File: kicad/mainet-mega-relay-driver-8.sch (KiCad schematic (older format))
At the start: 8 parts, among them J37 Screw_Terminal_01x03, K8 SANYOU_SRD_Form_C, Q8 2N3904, U9 4N37

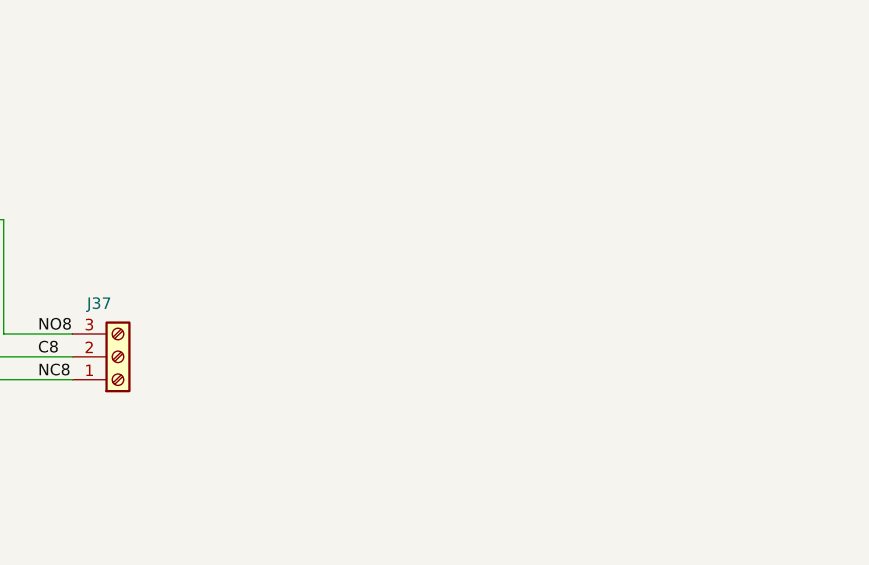
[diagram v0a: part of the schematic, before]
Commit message: KICAD: Agregar .sch para usar  el relé 8 para inhibir el M400  desde el software
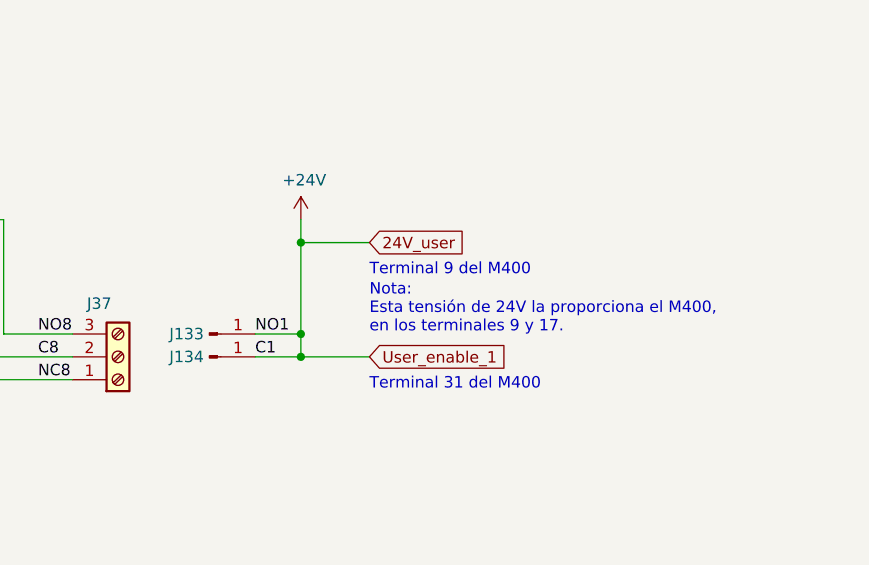
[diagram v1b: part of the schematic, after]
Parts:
- added J133, J134: Conn_01x01_Male, symbol Connector:Conn_01x01_Male
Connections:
- new net +24V: J133.1 (Pin_1), J134.1 (Pin_1)
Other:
- note added: "Nota:\nEsta tensión de 24V la proporciona el M400, \nen los terminales 9 y 17."
- note added: "Terminal 31 del M400"
- note added: "Terminal 9 del M400"
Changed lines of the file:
@@
 Text Notes 6000 5000 0    50   ~ 0
 Relay Ground\nNo conectar a la tierra\ndel Arduino Mega\n
+$Comp
+L Connector:Conn_01x01_Male J?
+U 1 1 6106E50A
+P 8550 3800
+AR Path="/5FC25793/5FD90A95/6106E50A" Ref="J?"  Part="1"
+AR Path="/5FC25793/5FD90D3E/6106E50A" Ref="J?"  Part="1"
+AR Path="/5FC25793/5FD92195/6106E50A" Ref="J133"  Part="1"
+F 0 "J133" H 8450 3800 50  0000 C CNN
+F 1 "Conn_01x01_Male" H 8658 3890 50  0001 C CNN
+F 2 "" H 8550 3800 50  0001 C CNN
+F 3 "~" H 8550 3800 50  0001 C CNN
+	1    8550 3800
+	1    0    0    -1
+$EndComp
+$Comp
+L Connector:Conn_01x01_Male J?
+U 1 1 6106E510
+P 8550 3900
+AR Path="/5FC25793/5FD90A95/6106E510" Ref="J?"  Part="1"
+AR Path="/5FC25793/5FD90D3E/6106E510" Ref="J?"  Part="1"
+AR Path="/5FC25793/5FD92195/6106E510" Ref="J134"  Part="1"
+F 0 "J134" H 8450 3900 50  0000 C CNN
+F 1 "Conn_01x01_Male" H 8658 3990 50  0001 C CNN
+F 2 "" H 8550 3900 50  0001 C CNN
+F 3 "~" H 8550 3900 50  0001 C CNN
+	1    8550 3900
+	1    0    0    -1
+$EndComp
+$Comp
+L power:+24V #PWR?
+U 1 1 6106E516
+P 8950 3300
+AR Path="/5FC25793/5FD90A95/6106E516" Ref="#PWR?"  Part="1"
+AR Path="/5FC25793/5FD90D3E/6106E516" Ref="#PWR?"  Part="1"
+AR Path="/5FC25793/5FD92195/6106E516" Ref="#PWR0113"  Part="1"
+F 0 "#PWR0113" H 8950 3150 50  0001 C CNN
+F 1 "+24V" H 8965 3473 50  0000 C CNN
+F 2 "" H 8950 3300 50  0001 C CNN
+F 3 "" H 8950 3300 50  0001 C CNN
+	1    8950 3300
+	1    0    0    -1
+$EndComp
+Wire Wire Line
+	8950 3300 8950 3400
+Wire Wire Line
+	8950 3800 8750 3800
+Text Label 8750 3800 0    50   ~ 0
+NO1
+Text Label 8750 3900 0    50   ~ 0
+C1
+Wire Wire Line
+	8750 3900 8950 3900
+Text Notes 9250 4050 0    50   ~ 0
+Terminal 31 del M400
+Text GLabel 9250 3400 2    50   Input ~ 0
+24V_user
+Wire Wire Line
+	8950 3400 9250 3400
+Connection ~ 8950 3400
+Wire Wire Line
+	8950 3400 8950 3800
+Text Notes 9250 3550 0    50   ~ 0
+Terminal 9 del M400
+Text Notes 9250 3800 0    50   ~ 0
+Nota:\nEsta tensión de 24V la proporciona el M400, \nen los terminales 9 y 17.
+Text GLabel 9250 3900 2    50   Input ~ 0
+User_enable_1
+Wire Wire Line
+	8950 3800 8950 3900
+Connection ~ 8950 3800
+Connection ~ 8950 3900
+Wire Wire Line
+	8950 3900 9250 3900
 $EndSCHEMATC
